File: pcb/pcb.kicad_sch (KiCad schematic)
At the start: 65 parts, among them J1 AudioJack4, J2 USB_C_Receptacle_USB2.0, SW1 Switch, SW10 Switch, SW11 Switch, SW12 Switch, SW13 Switch, SW14 Switch, SW15 Switch, SW16 Switch, SW17 Switch, SW18 Switch, SW2 Switch, SW3 Switch, SW4 Switch, SW5 Switch, SW6 Switch, SW7 Switch, SW8 Switch, SW9 Switch, U1 MCU_rp2040-zero, U2 MCU_rp2040-zero, U3 RollerEncoder_EVQWGD001

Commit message: v2
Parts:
- removed D15, D16, D17: D_Small, zzkeeb:Diode_1N4148-SOD123-reversible-flip3d, symbol Device:D_Small
- removed H1, H2, H3, H4: MountingHole, zzkeeb:Hole_M2-spacer, symbol Mechanical:MountingHole
- removed J2: USB_C_Receptacle_USB2.0, zzkeeb:Connector_USB-C-mid-mount-ali-reversible-data, symbol Connector:USB_C_Receptacle_USB2.0
- removed LED15: LED_SK6812MINI-E, zzkeeb:LED_SK6812-MINI-E-reversible, symbol zzkeeb:LED_SK6812MINI-E
- removed RE1: RotaryEncoder_Switch, zzkeeb:RotaryEncoder_EC11-reversible, symbol Device:RotaryEncoder_Switch
- removed SW15, SW16: Switch, zzkeeb:Switch_ChocV1-hotswap-reversible, symbol zzkeeb:Switch
- removed U3: RollerEncoder_EVQWGD001, zzkeeb:RotaryEncoder_EVQWGD001, symbol zzkeeb:RollerEncoder_EVQWGD001
- added D1: Diode, zzkeeb:Diode_1N4148-SOD123-reversible-flip3d, symbol zzkeeb:Diode
- added D18: Diode, zzkeeb:Diode_1N4148-SOD123-reversible-flip3d, symbol Diode:1N4148
- added FiveWay1: 5Way-Tactile_K1-1506DN-01, zzkeeb:Button_5way-reversible, symbol fingerpunch:5Way-Tactile_K1-1506DN-01
- added SW1: Switch, zzkeeb:Switch_ChocV1-hotswap-reversible, symbol zzkeeb:Switch
- added USB1 (x2): Connector_HRO-TYPE-C-31-M-12, zzkeeb:Connector_HRO-TYPE-C-31-M-12-data, symbol zzkeeb:Connector_HRO-TYPE-C-31-M-12
- D10: renamed from D9; value D_Small -> Diode; symbol Device:D_Small -> zzkeeb:Diode; col (none) -> 4; row (none) -> 1
- D11: renamed from D10; value D_Small -> Diode; symbol Device:D_Small -> zzkeeb:Diode; col (none) -> 0; row (none) -> 2
- D12: renamed from D11; value D_Small -> Diode; symbol Device:D_Small -> zzkeeb:Diode; col (none) -> 1; row (none) -> 2
- D13: renamed from D12; value D_Small -> Diode; symbol Device:D_Small -> zzkeeb:Diode; col (none) -> 2; row (none) -> 2
- D14: renamed from D13; value D_Small -> Diode; symbol Device:D_Small -> zzkeeb:Diode; col (none) -> 3; row (none) -> 2
- D15: renamed from D14; value D_Small -> Diode; symbol Device:D_Small -> zzkeeb:Diode; col (none) -> 4; row (none) -> 2
- D16: renamed from D18; value D_Small -> Diode; symbol Device:D_Small -> zzkeeb:Diode; col (none) -> 3; row (none) -> 3
- D17: renamed from D19; value D_Small -> Diode; symbol Device:D_Small -> zzkeeb:Diode; col (none) -> 4; row (none) -> 3
- D2: renamed from D1; value D_Small -> Diode; symbol Device:D_Small -> zzkeeb:Diode; col (none) -> 1; row (none) -> 0
- D3: renamed from D2; value D_Small -> Diode; symbol Device:D_Small -> zzkeeb:Diode; col (none) -> 2; row (none) -> 0
- D4: renamed from D3; value D_Small -> Diode; symbol Device:D_Small -> zzkeeb:Diode; col (none) -> 3; row (none) -> 0
- D5: renamed from D4; value D_Small -> Diode; symbol Device:D_Small -> zzkeeb:Diode; col (none) -> 4; row (none) -> 0
- D6: renamed from D5; value D_Small -> Diode; symbol Device:D_Small -> zzkeeb:Diode; col (none) -> 0; row (none) -> 1
- D7: renamed from D6; value D_Small -> Diode; symbol Device:D_Small -> zzkeeb:Diode; col (none) -> 1; row (none) -> 1
- D8: renamed from D7; value D_Small -> Diode; symbol Device:D_Small -> zzkeeb:Diode; col (none) -> 2; row (none) -> 1
- D9: renamed from D8; value D_Small -> Diode; symbol Device:D_Small -> zzkeeb:Diode; col (none) -> 3; row (none) -> 1
- LED1, LED10, LED11, LED12, LED13, LED14, LED2, LED3, LED4, LED7: footprint zzkeeb:LED_SK6812-MINI-E-reversible -> zzkeeb:LED_SK6812-MINI-E-reversible-flip3d
- LED15: renamed from LED18; footprint zzkeeb:LED_SK6812-MINI-E-reversible -> zzkeeb:LED_SK6812-MINI-E-reversible-flip3d
- LED16: renamed from LED17; footprint zzkeeb:LED_SK6812-MINI-E-reversible -> zzkeeb:LED_SK6812-MINI-E-reversible-flip3d
- LED17: renamed from LED16; footprint zzkeeb:LED_SK6812-MINI-E-reversible -> zzkeeb:LED_SK6812-MINI-E-reversible-flip3d
- LED5: renamed from LED9; footprint zzkeeb:LED_SK6812-MINI-E-reversible -> zzkeeb:LED_SK6812-MINI-E-reversible-flip3d
- LED6: renamed from LED8; footprint zzkeeb:LED_SK6812-MINI-E-reversible -> zzkeeb:LED_SK6812-MINI-E-reversible-flip3d
- LED8: renamed from LED6; footprint zzkeeb:LED_SK6812-MINI-E-reversible -> zzkeeb:LED_SK6812-MINI-E-reversible-flip3d
- LED9: renamed from LED5; footprint zzkeeb:LED_SK6812-MINI-E-reversible -> zzkeeb:LED_SK6812-MINI-E-reversible-flip3d
- SW10: renamed from SW9; col (none) -> 4; row (none) -> 1
- SW11: renamed from SW10; col (none) -> 0; row (none) -> 2
- SW12: renamed from SW11; col (none) -> 1; row (none) -> 2
- SW13: renamed from SW12; col (none) -> 2; row (none) -> 2
- SW14: renamed from SW13; col (none) -> 3; row (none) -> 2
- SW15: renamed from SW14; col (none) -> 4; row (none) -> 2
- SW16: renamed from SW17; col (none) -> 3; row (none) -> 3
- SW17: renamed from SW18; col (none) -> 4; row (none) -> 3
- SW2: renamed from SW1; col (none) -> 1; row (none) -> 0
- SW3: renamed from SW2; col (none) -> 2; row (none) -> 0
- SW4: renamed from SW3; col (none) -> 3; row (none) -> 0
- SW5: renamed from SW4; col (none) -> 4; row (none) -> 0
- SW6: renamed from SW5; col (none) -> 0; row (none) -> 1
- SW7: renamed from SW6; col (none) -> 1; row (none) -> 1
- SW8: renamed from SW7; col (none) -> 2; row (none) -> 1
- SW9: renamed from SW8; col (none) -> 3; row (none) -> 1
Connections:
- net GND: now also USB1.1 (GND), USB1.1 (GND), USB1.12 (GND), USB1.12 (GND)
- net RX: now also USB1.5 (DN2), USB1.5 (DN2), USB1.7 (DN1), USB1.7 (DN1)
- net TX: now also USB1.6 (DP1), USB1.6 (DP1), USB1.8 (DP2), USB1.8 (DP2)
- net col0: now also FiveWay1.6, SW1.2
- net col1: now also FiveWay1.5
- net col2: now also FiveWay1.3
- net col3: now also FiveWay1.2
- net col4: now also FiveWay1.1
- net row0: now also D1.1 (K)
- net +5V: now reaches U1.23 (5V)
- net +5V: now also J1.T, LED10.1 (VDD), LED11.1 (VDD), LED12.1 (VDD), LED13.1 (VDD), LED14.1 (VDD), LED15.1 (VDD), LED16.1 (VDD), LED17.1 (VDD), LED2.1 (VDD), LED3.1 (VDD), LED4.1 (VDD), LED5.1 (VDD), LED6.1 (VDD), LED7.1 (VDD), LED8.1 (VDD), LED9.1 (VDD), U2.23 (5V), D18.2 (A), USB1.11 (VBUS), USB1.11 (VBUS), USB1.2 (VBUS), USB1.2 (VBUS)
- net ENCA: no longer names the net of U1.17 (26)
- net ENCA: no longer U2.7 (6)
- net ENCB renamed row4
- net row4: now also FiveWay1.4
- removed net VCC: J1.T, LED1.1 (VDD), LED10.1 (VDD), LED11.1 (VDD), LED12.1 (VDD), LED13.1 (VDD), LED14.1 (VDD), LED15.1 (VDD), LED16.1 (VDD), LED17.1 (VDD), LED2.1 (VDD), LED3.1 (VDD), LED4.1 (VDD), LED5.1 (VDD), LED6.1 (VDD), LED7.1 (VDD), LED8.1 (VDD), LED9.1 (VDD), U1.21 (3V3), U2.21 (3V3)
- new net: D1.2 (A), SW1.1
- new net: D18.1 (K), LED1.1 (VDD)
- no-connect marks 21 -> 27
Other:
- moved on the sheet: D10, D11, D12, D13, D14, D15, D16, D17, D2, D3, D4, D5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

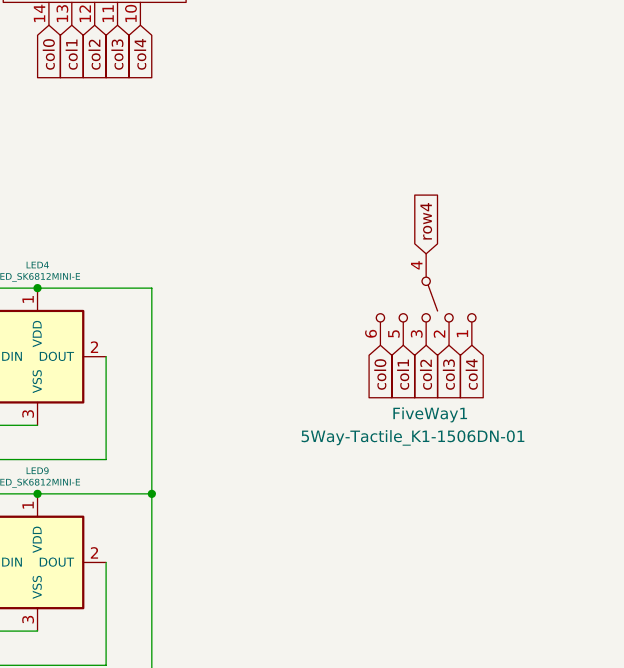
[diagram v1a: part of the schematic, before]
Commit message: use alps smd 5way
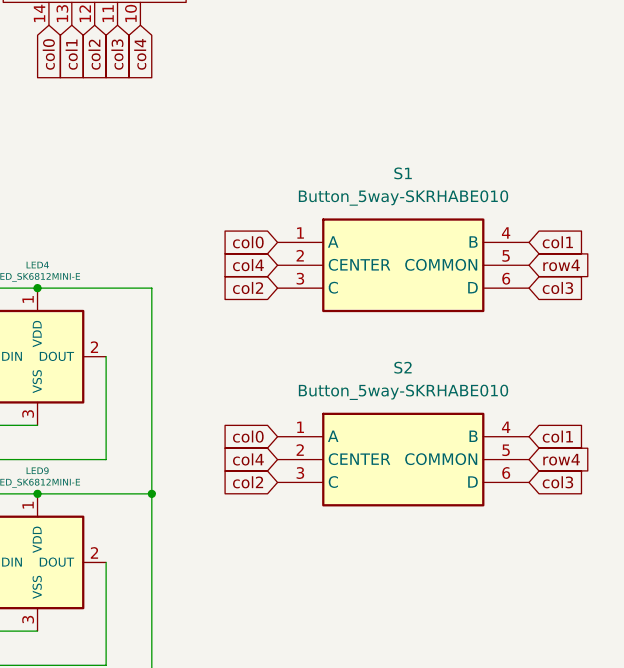
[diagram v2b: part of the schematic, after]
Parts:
- removed FiveWay1: 5Way-Tactile_K1-1506DN-01, zzkeeb:Button_5way-reversible, symbol fingerpunch:5Way-Tactile_K1-1506DN-01
- added S1, S2: Button_5way-SKRHABE010, zzkeeb:Button_5way-SKRHABE010, symbol zzkeeb:Button_5way-SKRHABE010
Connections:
- net col0: now also S1.1 (A), S2.1 (A)
- net col1: now also S1.4 (B), S2.4 (B)
- net col2: now also S1.3 (C), S2.3 (C)
- net col3: now also S1.6 (D), S2.6 (D)
- net col4: now also S1.2 (CENTER), S2.2 (CENTER)
- net row4: now also S1.5 (COMMON), S2.5 (COMMON)
